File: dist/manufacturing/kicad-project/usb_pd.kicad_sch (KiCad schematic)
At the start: 35 parts, among them J1 J1, Q1 Q1, Q2 Q2, Q3 Q3, U1 TPD4S480RUKR, U2 TPS26750SRSMR, U3 M24512-RMN6TP, U4 SN74LVC1G08DBVR

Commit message: Implement dual USB power/data ECO and consolidate industrial I/O
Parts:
- removed C72: 100nF, capacitor_cap0603, symbol Device:capacitor_down
- removed Q1: Q1, BSS123LT1G, symbol Custom:BSS123LT1G_NMOS
- removed Q2: Q2, CSD17484F4, symbol Custom:CSD17484F4_NMOS
- removed Q3: Q3, CSD17484F4, symbol Custom:CSD17484F4_NMOS
- removed R107: 1MΩ, resistor_res0603, symbol Device:boxresistor_down
- removed R108: 47kΩ, resistor_res0603, symbol Device:boxresistor_down
- added Q1: Q1, BSS123LT1G, symbol Custom:BSS123LT1G
- added Q2, Q3: CSD17484F4, CSD17484F4, symbol Device:U_CSD17484F4
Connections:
- net EPR_BLK_GATE: now also Q1.1 (G)
- net GND: now also Q2.2 (S), Q3.2 (S)
- net PD_INV_BASE: now also Q3.1 (G)
- net PD_LEVEL_BASE: now also Q2.1 (G)
- net PD_PATH_N: now also Q2.3 (D)
- net PD_PATH_OK: now also Q3.3 (D)
- net VBUS_LV: now also Q1.2 (S)
- net PD_SBU1_CONN: now reaches J1.10 (SBU1)
- net PD_SBU1_CONN: now also U1.1 (DP)
- net PD_SBU2_CONN: now reaches J1.16 (SBU2)
- net PD_SBU2_CONN: now also U1.2 (DM)
- removed net USB_DM_CONN: J1.12 (DM), J1.14 (DM), U1.2 (DM)
- net USB_DM_PROTECTED: no longer names the net of U1.14 (SBU2)
- removed net USB_DP_CONN: J1.11 (DP), J1.13 (DP), U1.1 (DP)
- net USB_DP_PROTECTED: no longer names the net of U1.15 (SBU1)
- net USB_VBUS renamed PD_VBUS
- net PD_VBUS: now also Q1.3 (D)
- no-connect marks 5 -> 9
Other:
- note added: "01 / USB-C PD POWER"
- note added: "J1 D+/D-: not connected. Q1: protected VBUS control. Q2/Q3: PD-path level translation."
- note added: "J1: dedicated 48 V / 5 A EPR sink. USB DATA is on J10; the two VBUS rails are separate."
- note added: "PD_SBU1_CONN"
- note added: "PD_SBU2_CONN"
- note added: "U1: 48 V CC/VBUS and unused SBU protection. U2: TPS26750 EPR sink controller. U3: PD policy EEPROM. U4: hardware power-permit gate."
- note removed: "01 / USB-C EPR Power and USB Data"
- note removed: "J1 carries 48 V / 5 A EPR power and USB 2.0 device data on one USB-C receptacle."
- note removed: "R107/R108/C72: 5-60 V attach sense. Q1: protected VBUS control. Q2/Q3: PD-path level translation."
- note removed: "U1: 48 V CC/VBUS and D+/D- protection. U2: TPS26750 EPR sink controller. U3: PD policy EEPROM. U4: hardware power-permit gate."
- note removed: "USB_DM_CONN"
- note removed: "USB_DM_PROTECTED"
- note removed: "USB_DP_CONN"
- note removed: "USB_DP_PROTECTED"
- note removed: "USB_VBUS_SENSE"

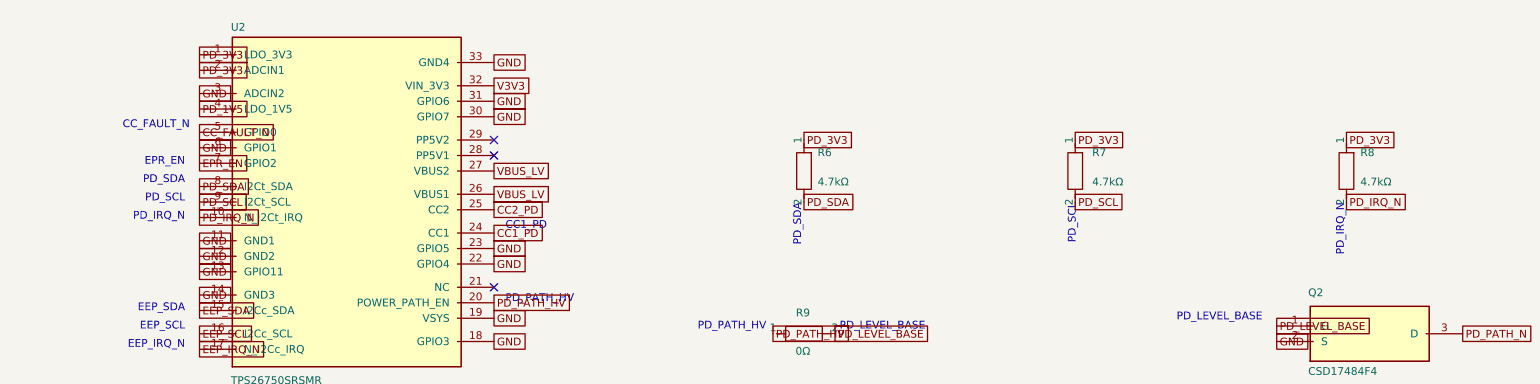
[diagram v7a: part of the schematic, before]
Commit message: Complete top-side routing and verify reference-board ECO
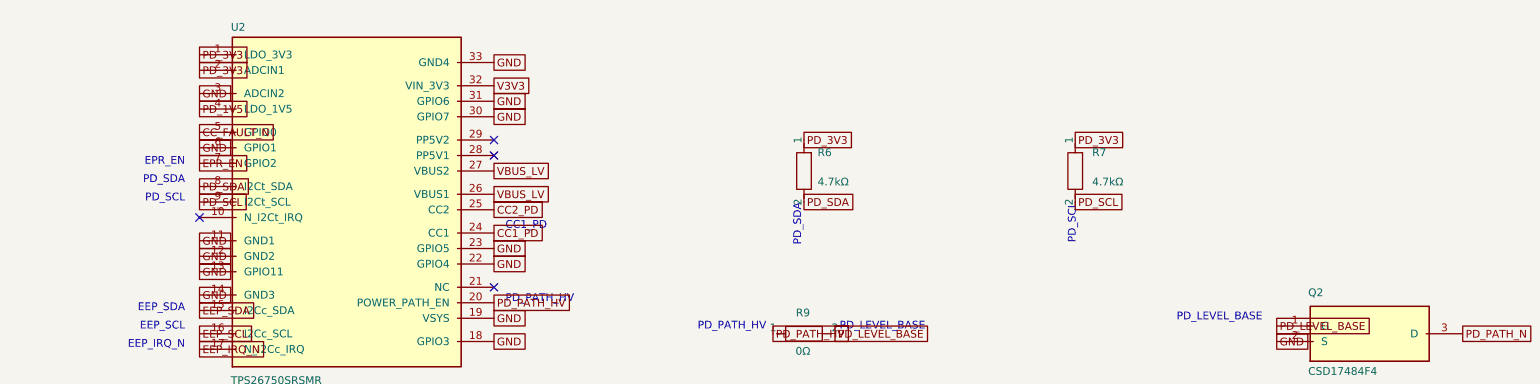
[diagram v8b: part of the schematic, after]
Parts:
- removed R8: 4.7kΩ, resistor_res0603, symbol Device:boxresistor_down
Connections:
- net PD_IRQ_N: no longer names the net of U2.10 (N_I2Ct_IRQ)
- no-connect marks 9 -> 10
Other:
- note removed: "PD_IRQ_N"
